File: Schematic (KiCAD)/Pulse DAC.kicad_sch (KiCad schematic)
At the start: 141 parts

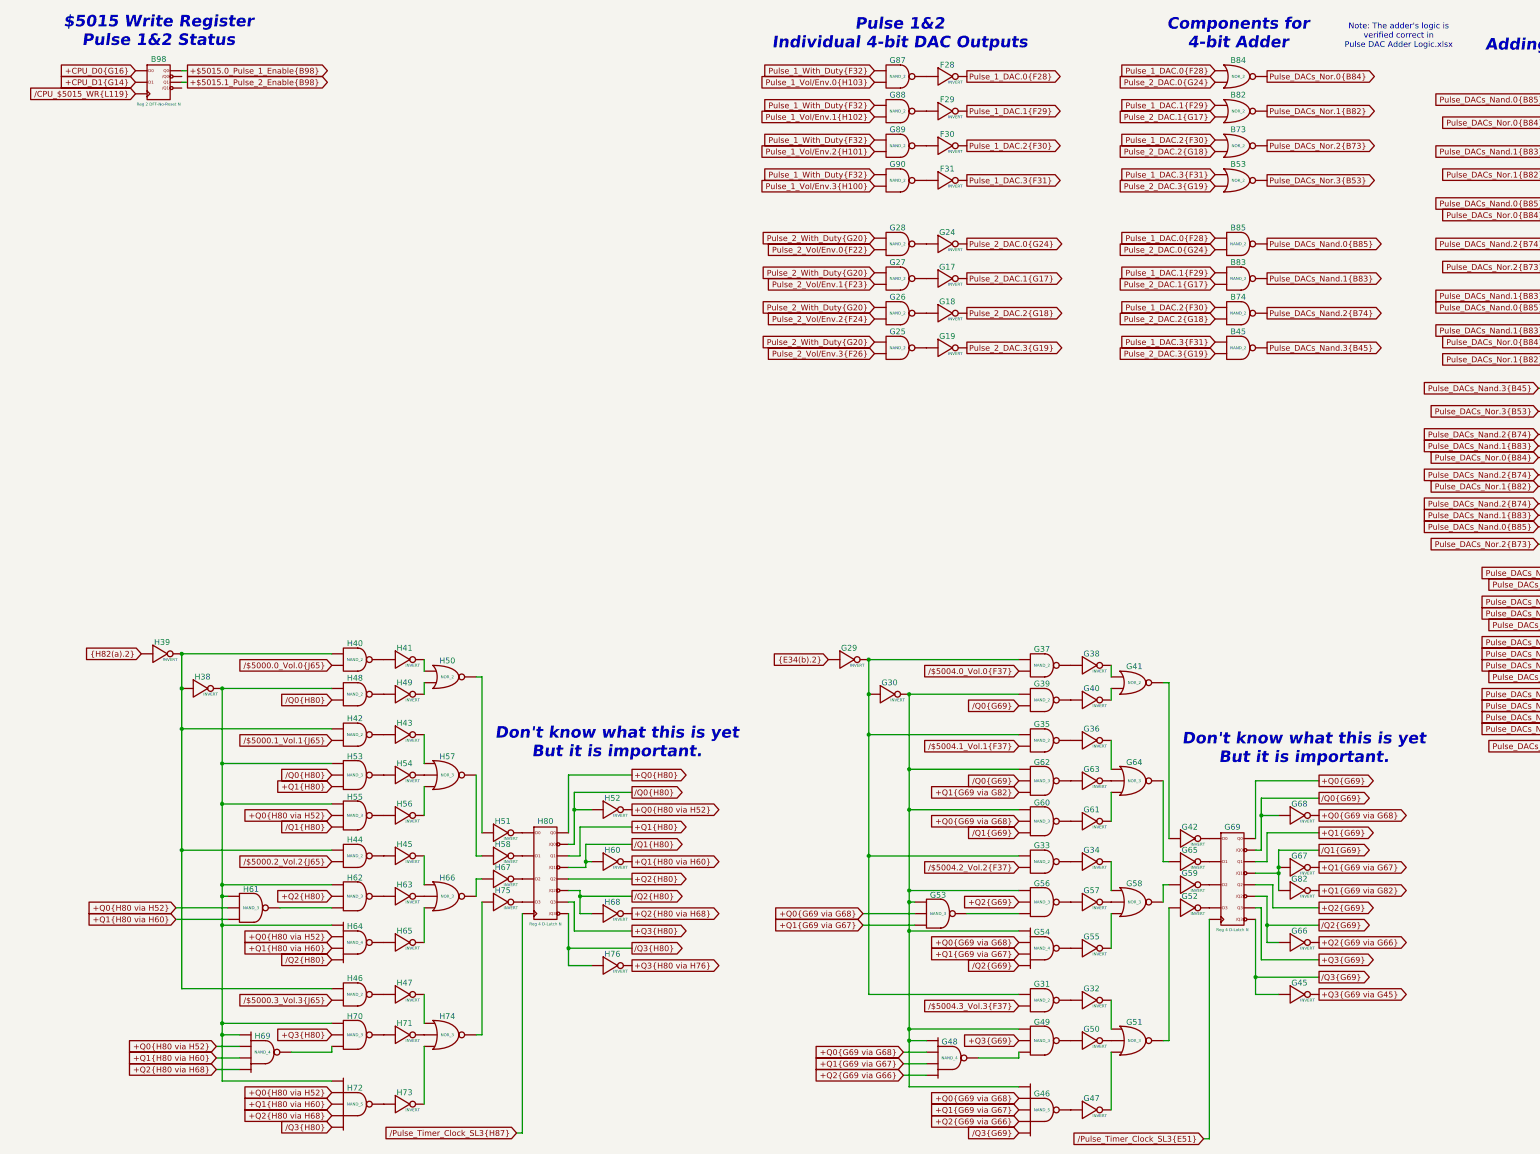
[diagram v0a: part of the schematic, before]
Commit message: - Lots of additional comments and signal name improvements.  - "Don't know what this is yet but it is important" section of the pulse channels:    - I worked out the logic and it is a 4-bit binary up-counter with preload, made from gates and D-latches instead of T-flip-flops.    - It is extremely similar to the envelope counter, but takes twice the die space and much more traces.    - None of its outputs go anywhere else, so I believe that it has no actual function.    - It seems to be a previous attempt at making the envelope counter and it got disconnected and left in.    - Each pulse channel has its own copy and I moved both of them to the "Artifacts" sheet.    - The wasted space amounts to about half of one of the large columns on the left side of the die.  - A couple of "OAI2" cells that noted "unclear order": I determined the correct order of the inputs based on several others which were known.  - Deduced the purpose of the 2 separate methods of scanline detection:    - The one looking for 3 consecutive reads finds the start of a scanline.    - The one counting PPU /RD to find PPU cycle 336, finds the end of the scanline.    - I moved these beside each other on the same sheet for clarity.  - A66.5 Changed from Nand to Nor in order to make sense.  - Basic test mode:    - Pin 92: Active low, enables test mode.    - Pin 29: In test mode, it gives external control of "Scanline Start Detection", which is normally done with the familiar 3 matching PPU reads.  When not in test mode, the pin has no function.    - Pin 30: In test mode, it gives external control of "Scanline End Detection", which is normally done by counting PPU /RD to find PPU cycle 336.  It also gives control of "Pulse Length Clock" when in test mode.  When not in test mode, the pin has no function.    - Pin 98/SL3: In test mode, it gives external control of "Pulse Timer Clock".  Whether or not in test mode, this pin low makes the MMC5 pretend $5104 had not yet been written since reset, probably as a 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
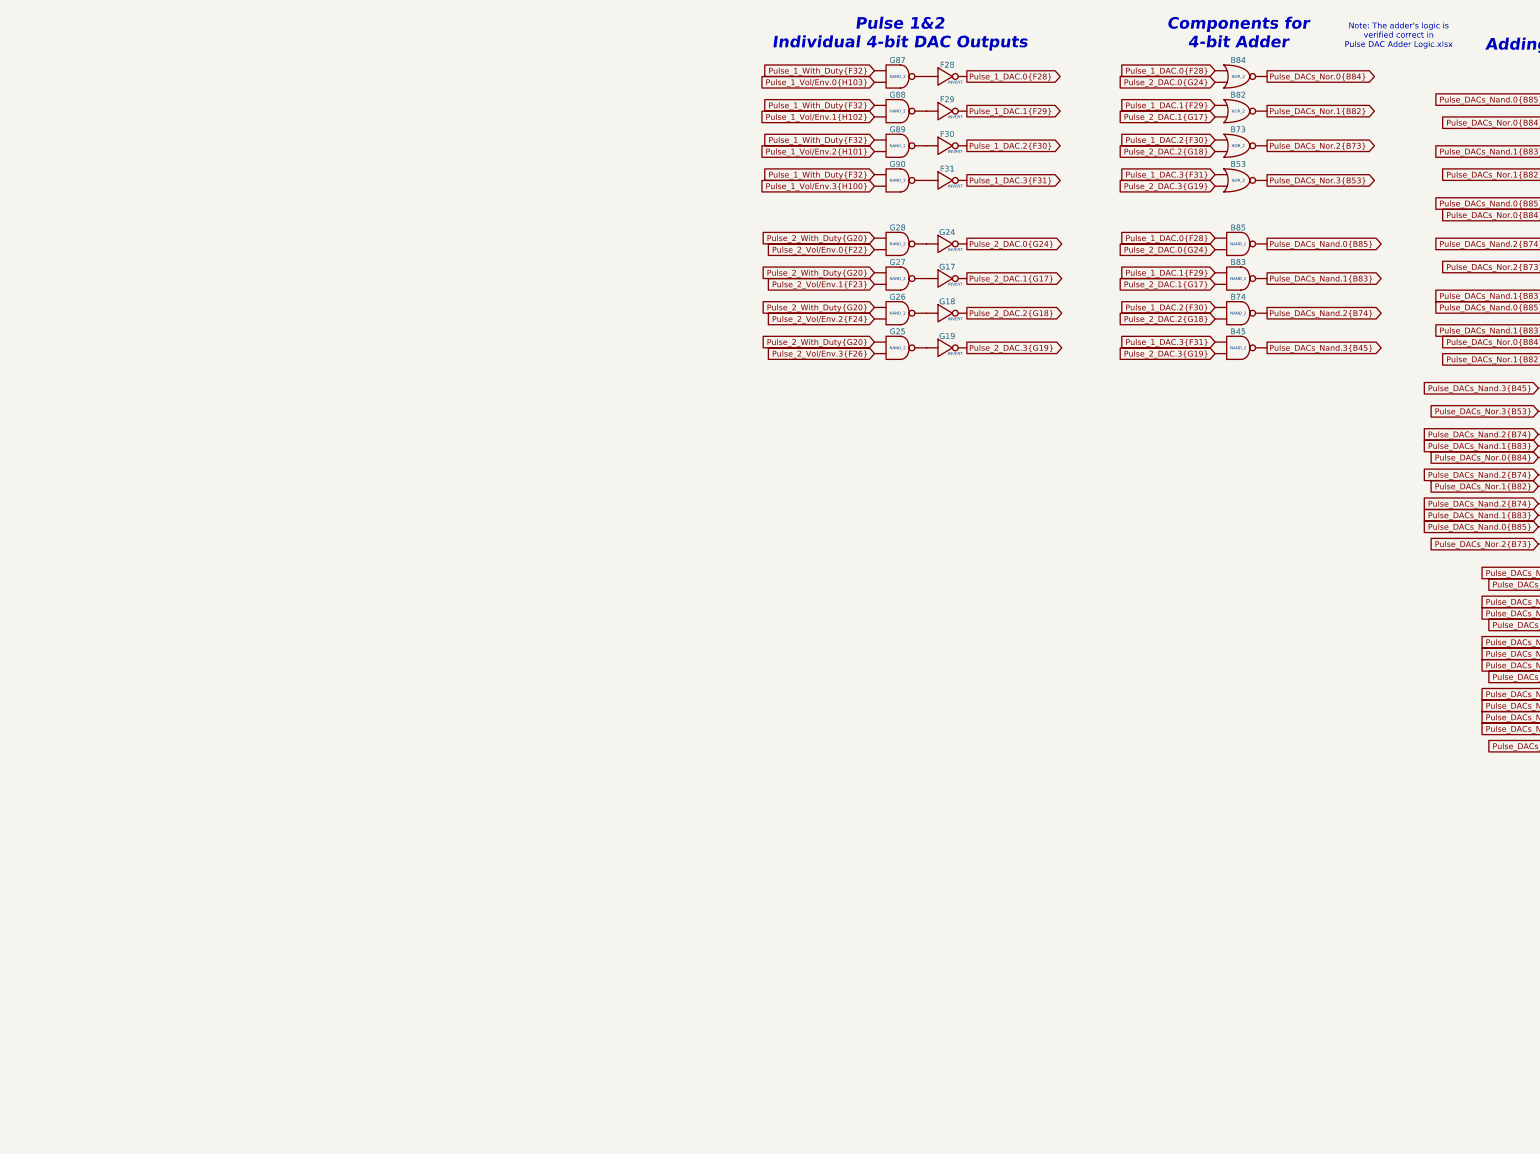
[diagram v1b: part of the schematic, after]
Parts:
- removed B98: Reg 2 DFF-No-Reset N, symbol MMC5:Reg_2_DFF-No-Reset_N
- removed G29, G30, G32, G34, G36, G38, G40, G42, G45, G47, G50, G52, G55, G57, G59, G61, G63, G65, G66, G67, G68, G82, H38, H39, H41, H43, H45, H47, H49, H51, H52, H54, H56, H58, H60, H63, H65, H67, H68, H71, H73, H75, H76: INVERT, symbol MMC5:INVERT
- removed G31, G33, G35, G37, G39, H40, H42, H44, H46, H48: NAND_2, symbol MMC5:NAND_2
- removed G41, H50: NOR_2, symbol MMC5:NOR_2
- removed G46, H72: NAND_5, symbol MMC5:NAND_5
- removed G48, G54, H64, H69: NAND_4, symbol MMC5:NAND_4
- removed G49, G53, G56, G60, G62, H53, H55, H61, H62, H70: NAND_3, symbol MMC5:NAND_3
- removed G51, G58, G64, H57, H66, H74: NOR_3, symbol MMC5:NOR_3
- removed G69, H80: Reg 4 D-Latch N, symbol MMC5:Reg_4_D-Latch_N
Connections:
- net at B59. (X): now also B61. (X); no longer B54. (X)
- net at B94. (X): now also B76. (X); no longer B75. (X)
- net at B89. (X): now also B77. (X); no longer B75. (X)
- net at B57. (X): now also B61. (X); no longer B56. (X)
- net at B71. (X): now also B70. (X); no longer B72. (X)
- net at B46. (X): now also B86. (X); no longer B47. (X)
- net at B63. (X): now also B62. (X); no longer B64. (X)
- net at B67. (X): now also B62. (X); no longer B68. (X)
- net at B58. (X): now also B61. (X); no longer B55. (X)
- net at B66. (X): now also B62. (X); no longer B65. (X)
- net at B79. (X): now also B78. (X); no longer B80. (X)
- net at B60. (X): now also B61. (X); no longer B52. (X)
- new net: F30. (X), G89. (X)
- new net: B54. (X), B59. (X)
- new net: B72. (X), B75. (X)
- new net: B75. (X), B94. (X)
- new net: B75. (X), B89. (X)
- new net: B86. (X), C13. (X)
- new net: B56. (X), B57. (X)
- new net: B78. (X), B88. (X)
- new net: B71. (X), B72. (X)
- new net: G18. (X), G26. (X)
- new net: B47. (X), B62. (X)
- new net: B46. (X), B47. (X)
- new net: G19. (X), G25. (X)
- new net: F29. (X), G88. (X)
- new net: G24. (X), G28. (X)
- new net: B63. (X), B64. (X)
- new net: B70. (X), B87. (X)
- new net: B80. (X), B81. (X)
- new net: B67. (X), B68. (X)
- new net: B55. (X), B58. (X)
- new net: B65. (X), B66. (X)
- new net: F28. (X), G87. (X)
- new net: B79. (X), B80. (X)
- new net: G17. (X), G27. (X)
- new net: B52. (X), B60. (X)
- new net: F31. (X), G90. (X)
- new net: B49. (X), B51. (X)
- new net: B49. (X), B50. (X)
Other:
- note removed: "$5015 Write Register Pulse 1&2 Status"
- note removed: "Don't know what this is yet But it is important."

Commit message: - Updated all of the various And-OR-Invert gates to have consistent names.  - Added the schematic for CL3 / SL3 GPIO pins.  There are no surprises revealed by this.  - Finished up the CPU address decoding tracing.  - Added one of the 'artifact' counters from the pulse channels
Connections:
- net at B59. (X): now also B61. (X); no longer B54. (X)
- net at B94. (X): now also B76. (X); no longer B75. (X)
- net at B89. (X): now also B77. (X); no longer B75. (X)
- net at B57. (X): now also B61. (X); no longer B56. (X)
- net at B71. (X): now also B70. (X); no longer B72. (X)
- net at B46. (X): now also B86. (X); no longer B47. (X)
- net at B63. (X): now also B62. (X); no longer B64. (X)
- net at B67. (X): now also B62. (X); no longer B68. (X)
- net at B58. (X): now also B61. (X); no longer B55. (X)
- net at B66. (X): now also B62. (X); no longer B65. (X)
- net at B79. (X): now also B78. (X); no longer B80. (X)
- net at B60. (X): now also B61. (X); no longer B52. (X)
- new net: F30. (X), G89. (X)
- new net: B54. (X), B59. (X)
- new net: B72. (X), B75. (X)
- new net: B75. (X), B94. (X)
- new net: B75. (X), B89. (X)
- new net: B86. (X), C13. (X)
- new net: B56. (X), B57. (X)
- new net: B78. (X), B88. (X)
- new net: B71. (X), B72. (X)
- new net: G18. (X), G26. (X)
- new net: B47. (X), B62. (X)
- new net: B46. (X), B47. (X)
- new net: G19. (X), G25. (X)
- new net: F29. (X), G88. (X)
- new net: G24. (X), G28. (X)
- new net: B63. (X), B64. (X)
- new net: B70. (X), B87. (X)
- new net: B80. (X), B81. (X)
- new net: B67. (X), B68. (X)
- new net: B55. (X), B58. (X)
- new net: B65. (X), B66. (X)
- new net: F28. (X), G87. (X)
- new net: B79. (X), B80. (X)
- new net: G17. (X), G27. (X)
- new net: B52. (X), B60. (X)
- new net: F31. (X), G90. (X)
- new net: B49. (X), B51. (X)
- new net: B49. (X), B50. (X)
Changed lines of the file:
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@@
 	)
 	(symbol
-		(lib_name "NAND_2_6")
+		(lib_name "NAND_2_19")
 		(lib_id "MMC5:NAND_2")
 		(at 209.55 44.45 0)
@@
 	)
 	(symbol
-		(lib_name "NOR_3_3")
 		(lib_id "MMC5:NOR_3")
 		(at 378.46 86.36 0)
@@
 	)
 	(symbol
-		(lib_name "INVERT_43")
+		(lib_name "INVERT_22")
 		(lib_id "MMC5:INVERT")
 		(at 355.6 102.87 0)
@@
 	)
 	(symbol
-		(lib_name "INVERT_14")
+		(lib_name "INVERT_23")
 		(lib_id "MMC5:INVERT")
 		(at 379.73 157.48 0)
@@
 	)
 	(symbol
-		(lib_name "INVERT_12")
+		(lib_name "INVERT_24")
 		(lib_id "MMC5:INVERT")
 		(at 379.73 139.7 0)
@@
 	)
 	(symbol
-		(lib_name "NAND_2_18")
+		(lib_name "NAND_2_3")
 		(lib_id "MMC5:NAND_2")
 		(at 284.48 73.66 0)
@@
 	)
 	(symbol
-		(lib_name "NAND_2_19")
+		(lib_name "NAND_2_7")
 		(lib_id "MMC5:NAND_2")
 		(at 358.14 86.36 0)
@@
 	)
 	(symbol
-		(lib_name "INVERT_45")
+		(lib_name "INVERT_10")
 		(lib_id "MMC5:INVERT")
 		(at 358.14 50.8 0)
@@
 	)
 	(symbol
-		(lib_name "INVERT_35")
 		(lib_id "MMC5:INVERT")
 		(at 378.46 68.58 0)
@@
 	)
 	(symbol
-		(lib_name "NOR_2_5")
+		(lib_name "NOR_2_1")
 		(lib_id "MMC5:NOR_2")
 		(at 284.48 44.45 0)
@@
 	)
 	(symbol
-		(lib_name "XOR_2_1")
+		(lib_name "XOR_2_2")
 		(lib_id "MMC5:XOR_2")
 		(at 389.89 77.47 0)
@@
 	)
 	(symbol
-		(lib_name "INVERT_18")
+		(lib_name "INVERT_5")
 		(lib_id "MMC5:INVERT")
 		(at 220.98 81.28 0)
@@
 	)
 	(symbol
-		(lib_name "XOR_2_2")
+		(lib_name "XOR_2_1")
 		(lib_id "MMC5:XOR_2")
 		(at 389.89 110.49 0)
@@
 	)
 	(symbol
+		(lib_name "NOR_2_3")
 		(lib_id "MMC5:NOR_2")
 		(at 284.48 29.21 0)
@@
 	)
 	(symbol
-		(lib_name "NAND_2_8")
+		(lib_name "NAND_2_4")
 		(lib_id "MMC5:NAND_2")
 		(at 209.55 88.9 0)
@@
 	)
 	(symbol
-		(lib_name "INVERT_5")
+		(lib_name "INVERT_9")
 		(lib_id "MMC5:INVERT")
 		(at 220.98 36.83 0)
@@
 	)
 	(symbol
-		(lib_name "NAND_2_14")
+		(lib_name "NAND_2_5")
 		(lib_id "MMC5:NAND_2")
 		(at 209.55 66.04 0)
@@
 	)
 	(symbol
-		(lib_name "NAND_2_5")
 		(lib_id "MMC5:NAND_2")
 		(at 284.48 88.9 0)
@@
 	)
 	(symbol
-		(lib_name "INVERT_41")
+		(lib_name "INVERT_8")
 		(lib_id "MMC5:INVERT")
 		(at 367.03 118.11 0)
@@
 	)
 	(symbol
-		(lib_name "INVERT_38")
+		(lib_name "INVERT_4")
 		(lib_id "MMC5:INVERT")
 		(at 358.14 71.12 0)
@@
 	)
 	(symbol
-		(lib_name "NOR_2_3")
 		(lib_id "MMC5:NOR_2")
 		(at 358.14 58.42 0)
@@
 	)
 	(symbol
-		(lib_name "INVERT_42")
+		(lib_name "INVERT_3")
 		(lib_id "MMC5:INVERT")
 		(at 367.03 125.73 0)
@@
 	)
 	(symbol
-		(lib_name "NAND_2_23")
+		(lib_name "NAND_2_6")
 		(lib_id "MMC5:NAND_2")
 		(at 367.03 100.33 0)
@@
 	)
 	(symbol
-		(lib_name "NAND_2_15")
+		(lib_name "NAND_2_10")
 		(lib_id "MMC5:NAND_2")
 		(at 284.48 81.28 0)
@@
 	)
 	(symbol
-		(lib_name "NAND_3_4")
+		(lib_name "NAND_3_2")
 		(lib_id "MMC5:NAND_3")
 		(at 368.3 147.32 0)
@@
 	)
 	(symbol
-		(lib_name "NAND_2_20")
+		(lib_name "NAND_2_8")
 		(lib_id "MMC5:NAND_2")
 		(at 358.14 78.74 0)
@@
 	)
 	(symbol
-		(lib_name "NAND_2_7")
+		(lib_name "NAND_2_1")
 		(lib_id "MMC5:NAND_2")
 		(at 209.55 81.28 0)
@@
 	)
 	(symbol
-		(lib_name "NAND_3_7")
+		(lib_name "NAND_3_1")
 		(lib_id "MMC5:NAND_3")
 		(at 355.6 125.73 0)
@@
 	)
 	(symbol
-		(lib_name "NAND_2_1")
+		(lib_name "NAND_2_9")
 		(lib_id "MMC5:NAND_2")
 		(at 284.48 66.04 0)
@@
 	)
 	(symbol
-		(lib_name "INVERT_19")
+		(lib_name "INVERT_11")
 		(lib_id "MMC5:INVERT")
 		(at 220.98 44.45 0)
@@
 	)
 	(symbol
-		(lib_name "INVERT_40")
+		(lib_name "INVERT_12")
 		(lib_id "MMC5:INVERT")
 		(at 367.03 110.49 0)
@@
 	)
 	(symbol
-		(lib_name "INVERT_37")
+		(lib_name "INVERT_7")
 		(lib_id "MMC5:INVERT")
 		(at 369.57 86.36 0)
@@
 	)
 	(symbol
-		(lib_name "INVERT_3")
+		(lib_name "INVERT_6")
 		(lib_id "MMC5:INVERT")
 		(at 220.98 29.21 0)
@@
 	)
 	(symbol
-		(lib_name "NAND_2_4")
+		(lib_name "NAND_2_2")
 		(lib_id "MMC5:NAND_2")
 		(at 368.3 139.7 0)
@@
 	)
 	(symbol
-		(lib_name "NOR_2_4")
+		(lib_name "NOR_2_2")
 		(lib_id "MMC5:NOR_2")
 		(at 284.48 52.07 0)
@@
 	)
 	(symbol
-		(lib_name "NAND_2_2")
+		(lib_name "NAND_2_11")
 		(lib_id "MMC5:NAND_2")
 		(at 209.55 29.21 0)
@@
 	)
 	(symbol
-		(lib_name "NAND_2_22")
+		(lib_name "NAND_2_12")
 		(lib_id "MMC5:NAND_2")
 		(at 355.6 118.11 0)
@@
 	)
 	(symbol
-		(lib_name "INVERT_16")
+		(lib_name "INVERT_13")
 		(lib_id "MMC5:INVERT")
 		(at 220.98 88.9 0)
@@
 	)
 	(symbol
-		(lib_name "INVERT_4")
+		(lib_name "INVERT_1")
 		(lib_id "MMC5:INVERT")
 		(at 220.98 73.66 0)
@@
 	)
 	(symbol
-		(lib_name "NAND_2_16")
+		(lib_name "NAND_2_13")
 		(lib_id "MMC5:NAND_2")
 		(at 209.55 36.83 0)
@@
 	)
 	(symbol
-		(lib_name "NAND_4_2")
 		(lib_id "MMC5:NAND_4")
 		(at 368.3 168.91 0)
@@
 	)
 	(symbol
-		(lib_name "INVERT_36")
+		(lib_name "INVERT_14")
 		(lib_id "MMC5:INVERT")
 		(at 369.57 78.74 0)
@@
 	)
 	(symbol
-		(lib_name "NAND_2_9")
+		(lib_name "NAND_2_14")
 		(lib_id "MMC5:NAND_2")
 		(at 209.55 52.07 0)
@@
 	)
 	(symbol
-		(lib_name "INVERT_13")
+		(lib_name "INVERT_15")
 		(lib_id "MMC5:INVERT")
 		(at 379.73 147.32 0)
@@
 	)
 	(symbol
-		(lib_name "INVERT_15")
+		(lib_name "INVERT_16")
 		(lib_id "MMC5:INVERT")
 		(at 379.73 168.91 0)
@@
 	)
 	(symbol
+		(lib_name "INVERT_17")
 		(lib_id "MMC5:INVERT")
 		(at 378.46 36.83 0)
@@
 	)
 	(symbol
-		(lib_name "INVERT_1")
+		(lib_name "INVERT_18")
 		(lib_id "MMC5:INVERT")
 		(at 358.14 39.37 0)
@@
 	)
 	(symbol
-		(lib_name "NAND_2_24")
+		(lib_name "NAND_2_15")
 		(lib_id "MMC5:NAND_2")
 		(at 367.03 48.26 0)
@@
 	)
 	(symbol
-		(lib_name "INVERT_39")
+		(lib_name "INVERT_21")
 		(lib_id "MMC5:INVERT")
 		(at 378.46 100.33 0)
@@
 	)
 	(symbol
-		(lib_name "INVERT_17")
+		(lib_name "INVERT_20")
 		(lib_id "MMC5:INVERT")
 		(at 220.98 52.07 0)
@@
 	)
 	(symbol
-		(lib_name "INVERT_44")
+		(lib_name "INVERT_19")
 		(lib_id "MMC5:INVERT")
 		(at 378.46 48.26 0)
@@
 	)
 	(symbol
+		(lib_name "NAND_2_16")
 		(lib_id "MMC5:NAND_2")
 		(at 367.03 36.83 0)
@@
 	)
 	(symbol
-		(lib_name "NAND_2_17")
+		(lib_name "NAND_2_18")
 		(lib_id "MMC5:NAND_2")
 		(at 209.55 73.66 0)
@@
 	)
 	(symbol
-		(lib_name "NAND_2_21")
+		(lib_name "NAND_2_17")
 		(lib_id "MMC5:NAND_2")
 		(at 367.03 68.58 0)
@@
 	)
 	(symbol
-		(lib_name "NOR_2_1")
+		(lib_name "NOR_2_4")
 		(lib_id "MMC5:NOR_2")
 		(at 284.48 36.83 0)
